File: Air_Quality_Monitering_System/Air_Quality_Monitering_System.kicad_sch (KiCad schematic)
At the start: 54 parts, among them J1 USB_C_Receptacle_USB2.0_16P, J2 Conn_01x02_Pin, J3 Conn_01x03_Pin, J4 Conn_01x04_Pin, Q1 SS8050, Q2 SS8050, SW1 SW_Push, SW2 SW_Push, U1 CH340C, U2 MT3608, U3 AMS1117-3.3, U4 TP4056-42-ESOP8, U5 MQ-6, U6 ESP-12E

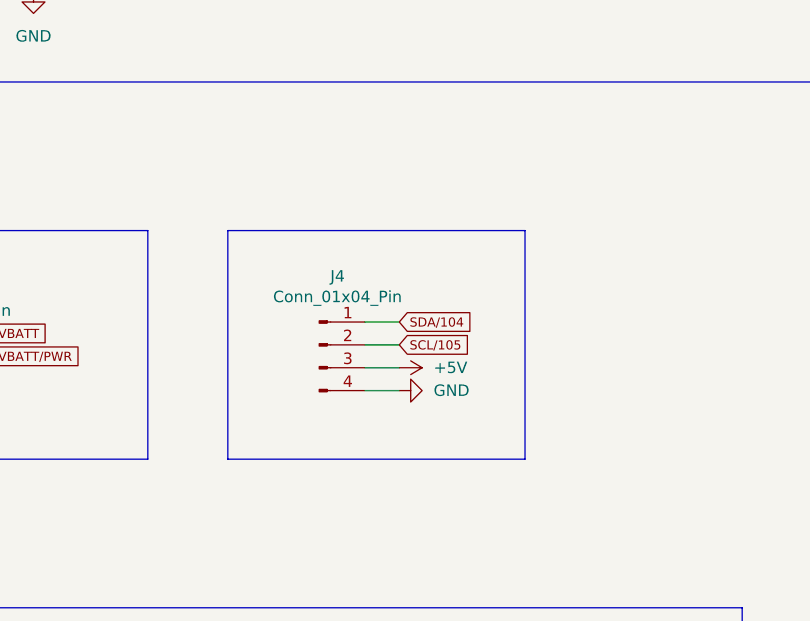
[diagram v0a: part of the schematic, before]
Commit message: Footprints are assigned
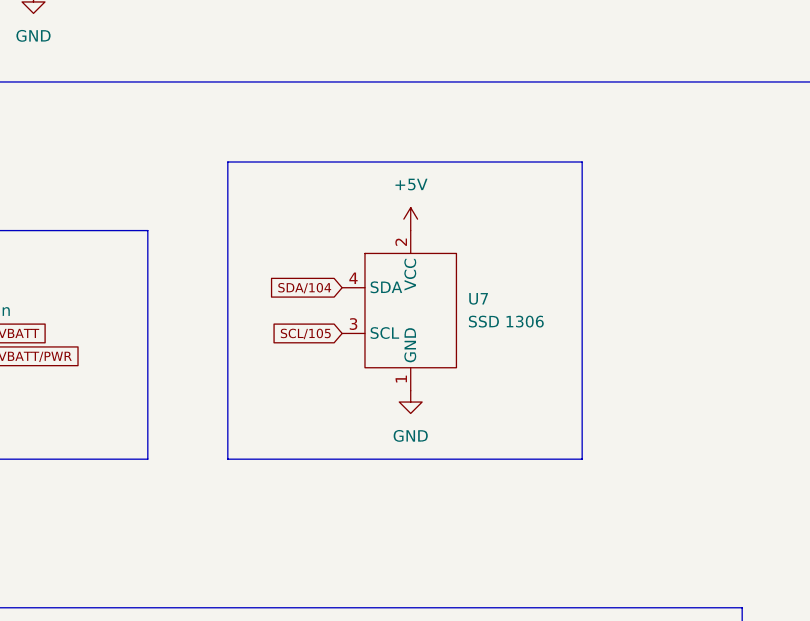
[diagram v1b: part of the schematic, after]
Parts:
- removed J4: Conn_01x04_Pin, symbol Connector:Conn_01x04_Pin
- added U7: SSD 1306, OLED SSD1306:SSD 1306, symbol OLED SSD1306:SSD_1306
- C1: footprint (none) -> Capacitor_SMD:CP_Elec_6.3x5.7
- C10, C11, C12, C13, C5: footprint (none) -> Capacitor_SMD:C_0603_1608Metric
- C2, C3, C4, C6, C7, C8, C9: footprint (none) -> Capacitor_SMD:C_0805_2012Metric
- D3, D4, D5: footprint (none) -> Diode_SMD:D_SOD-323
- D6, D7, D8, D9: footprint (none) -> Diode_SMD:D_0603_1608Metric
- J1: footprint (none) -> Connector_USB:USB_C_Receptacle_HRO_TYPE-C-31-M-12
- J2: footprint (none) -> Connector_PinHeader_2.54mm:PinHeader_1x02_P2.54mm_Vertical
- J3: footprint (none) -> Connector_PinHeader_2.54mm:PinHeader_1x03_P2.54mm_Vertical
- L1: footprint (none) -> Inductor_SMD:L_6.3x6.3_H3
- R1, R10, R11, R12, R13, R14, R15, R16, R17, R2, R3, R4, R5, R6, R7, R8, R9: footprint (none) -> Resistor_SMD:R_0603_1608Metric
- SW1, SW2: footprint (none) -> Button_Switch_SMD:SW_SPST_TL3342
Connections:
- net +5V: now also U7.2 (VCC)
- net GND: now also U7.1 (GND)
- net SCL/105: now also U7.3 (SCL)
- net SDA/104: now also U7.4 (SDA)
